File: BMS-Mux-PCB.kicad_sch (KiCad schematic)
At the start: 54 parts, among them J1 Conn_02x08_Counter_Clockwise, J2 Conn_02x08_Counter_Clockwise, J3 Conn_02x09_Counter_Clockwise, J4 Conn_01x18, J5 Conn_01x02, J6 Conn_02x10_Counter_Clockwise, Q1 BSS123, Q2 BSS123, U1 74CBTLV3257, U2 74CBTLV3257, U3 TMR_1-4812, U4 TEC2-4810WI

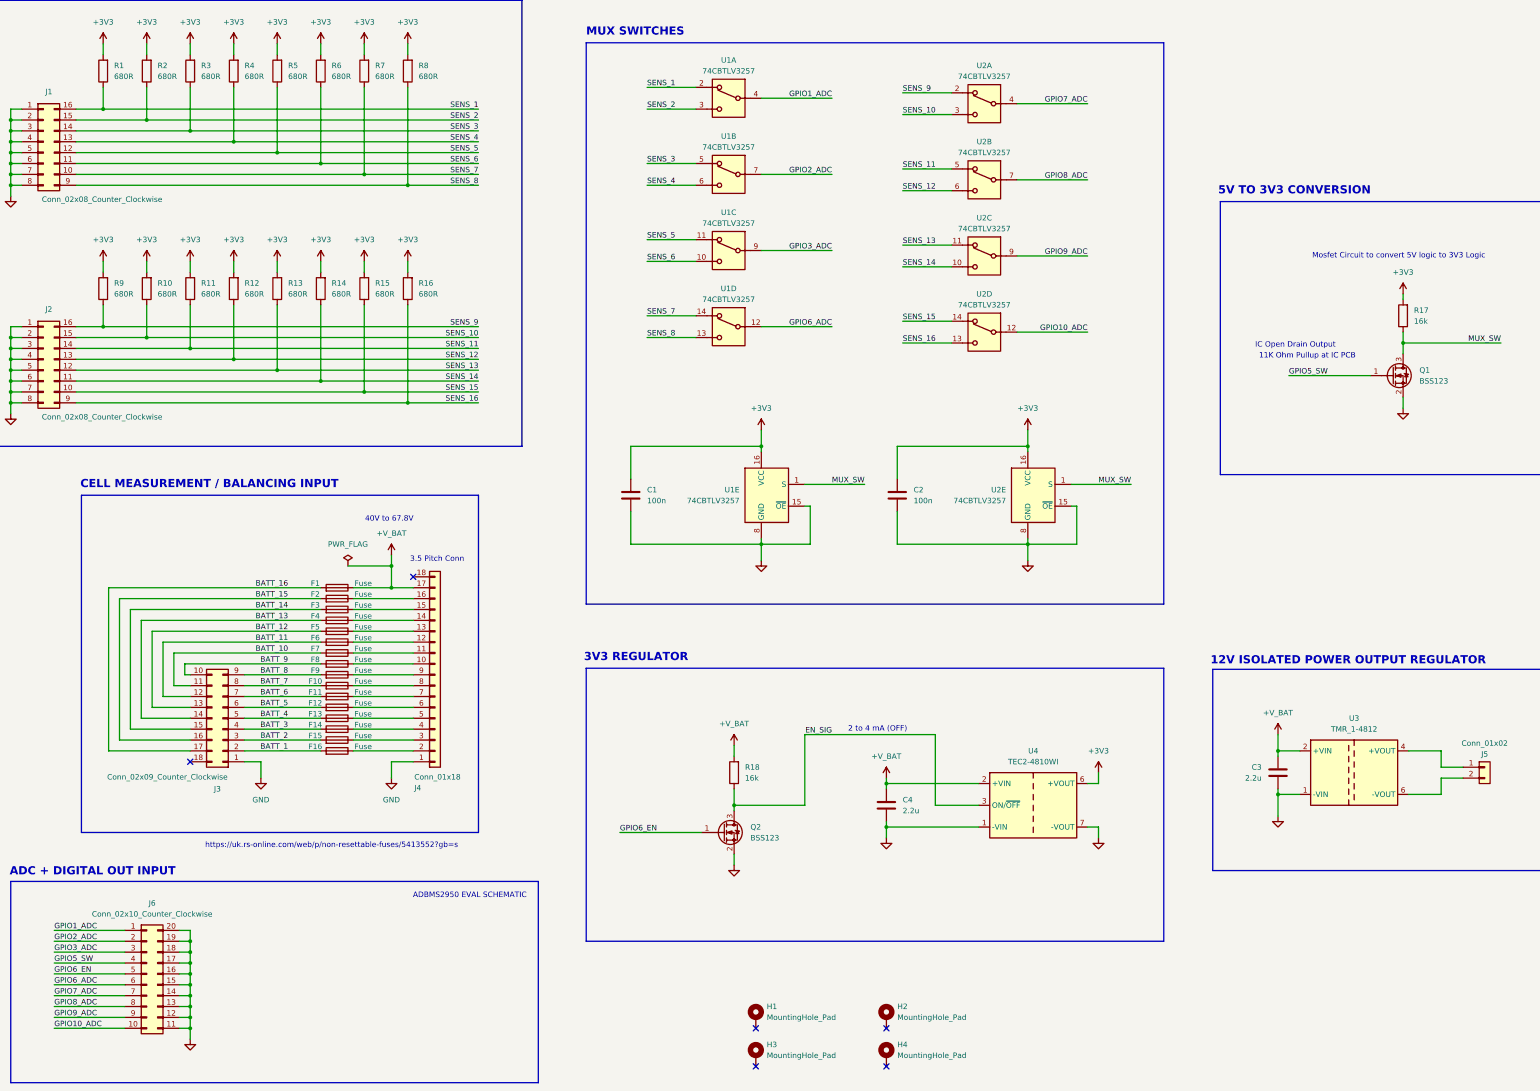
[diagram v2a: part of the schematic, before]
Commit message: updated footprints and started layout
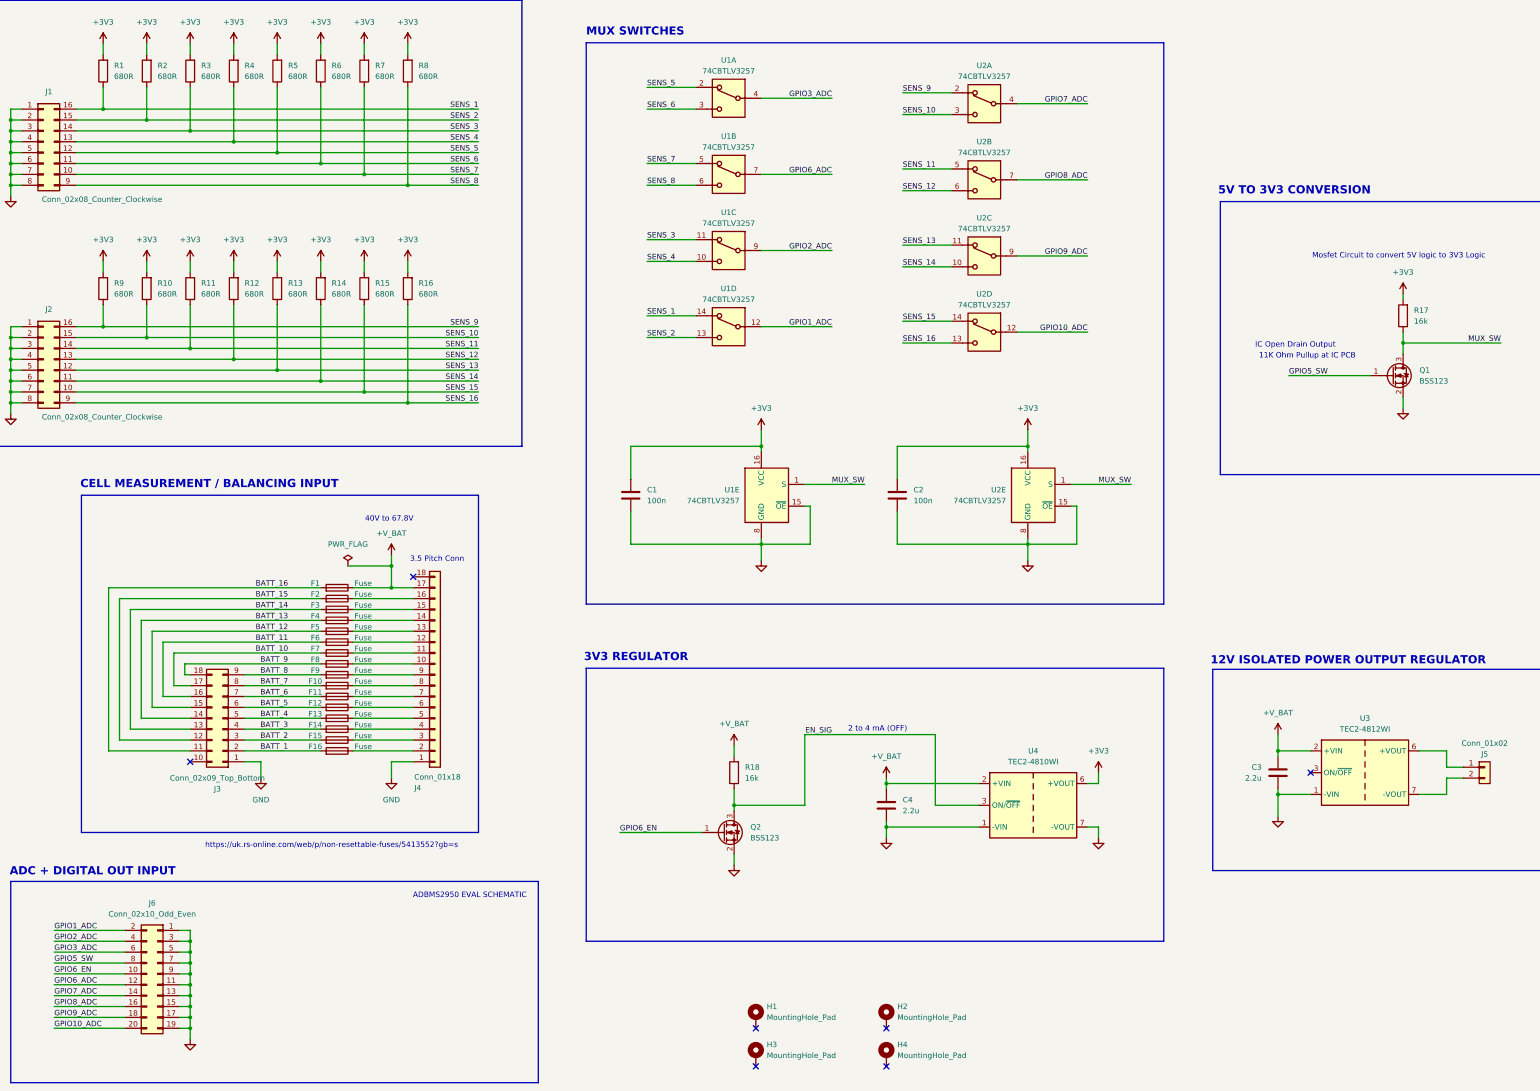
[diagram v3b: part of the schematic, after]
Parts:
- removed J3: Conn_02x09_Counter_Clockwise, Connector_Molex:Molex_Micro-Fit_3.0_43045-1800_2x09_P3.00mm_Horizontal, symbol Connector_Generic:Conn_02x09_Counter_Clockwise
- removed J6: Conn_02x10_Counter_Clockwise, Connector_PinHeader_2.54mm:PinHeader_2x10_P2.54mm_Vertical, symbol Connector_Generic:Conn_02x10_Counter_Clockwise
- removed U3: TMR_1-4812, Converter_DCDC:Converter_DCDC_TRACO_TMR-1-xxxx_Single_THT, symbol Regulator_Switching:TMR_1-4812
- added J3: Conn_02x09_Top_Bottom, BMS-Mux-footprints:Molex_Micro-Fit_3.0_43045-1800_2x09_P3.00mm_Horizontal, symbol Connector_Generic:Conn_02x09_Top_Bottom
- added J6: Conn_02x10_Odd_Even, Connector_PinHeader_2.54mm:PinHeader_2x10_P2.54mm_Vertical, symbol Connector_Generic:Conn_02x10_Odd_Even
- added U3: TEC2-4812WI, Converter_DCDC:Converter_DCDC_TRACO_TMR-xxxx_THT, symbol Converter_DCDC:TEC2-4812WI
- J1, J2: footprint Connector_Molex:Molex_Micro-Fit_3.0_43045-1600_2x08_P3.00mm_Horizontal -> BMS-Mux-footprints:Molex_Micro-Fit_3.0_43045-1600_2x08_P3.00mm_Horizontal
- J5: footprint Connector_Molex:Molex_Micro-Fit_3.0_43650-0200_1x02_P3.00mm_Horizontal -> BMS-Mux-footprints:Molex_Micro-Fit_3.0_43650-0200_1x02_P3.00mm_Horizontal
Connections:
- net +V_BAT: now also U3.2 (+VIN)
- net BATT_1: now also J3.2 (Pin_2)
- net BATT_10: now also J3.17 (Pin_17)
- net BATT_11: now also J3.16 (Pin_16)
- net BATT_12: now also J3.15 (Pin_15)
- net BATT_13: now also J3.14 (Pin_14)
- net BATT_14: now also J3.13 (Pin_13)
- net BATT_15: now also J3.12 (Pin_12)
- net BATT_16: now also J3.11 (Pin_11)
- net BATT_2: now also J3.3 (Pin_3)
- net BATT_3: now also J3.4 (Pin_4)
- net BATT_4: now also J3.5 (Pin_5)
- net BATT_5: now also J3.6 (Pin_6)
- net BATT_6: now also J3.7 (Pin_7)
- net BATT_7: now also J3.8 (Pin_8)
- net BATT_8: now also J3.9 (Pin_9)
- net BATT_9: now also J3.18 (Pin_18)
- net GND: now also J3.1 (Pin_1), J6.1 (Pin_1), J6.11 (Pin_11), J6.13 (Pin_13), J6.15 (Pin_15), J6.17 (Pin_17), J6.19 (Pin_19), J6.3 (Pin_3), J6.5 (Pin_5), J6.7 (Pin_7), J6.9 (Pin_9), U3.1 (-VIN)
- net GPIO10_ADC: now also J6.20 (Pin_20)
- net GPIO1_ADC: now also U1.12, J6.2 (Pin_2); no longer U1.4
- net GPIO2_ADC: now also U1.9, J6.4 (Pin_4); no longer U1.7
- net GPIO3_ADC: now also U1.4, J6.6 (Pin_6); no longer U1.9
- net GPIO5_SW: now also J6.8 (Pin_8)
- net GPIO6_ADC: now also U1.7, J6.12 (Pin_12); no longer U1.12
- net GPIO6_EN: now also J6.10 (Pin_10)
- net GPIO7_ADC: now also J6.14 (Pin_14)
- net GPIO8_ADC: now also J6.16 (Pin_16)
- net GPIO9_ADC: now also J6.18 (Pin_18)
- net SENS_1: now also U1.14; no longer U1.2
- net SENS_2: now also U1.13; no longer U1.3
- net SENS_3: now also U1.11; no longer U1.5
- net SENS_4: now also U1.10; no longer U1.6
- net SENS_5: now also U1.2; no longer U1.11
- net SENS_6: now also U1.3; no longer U1.10
- net SENS_7: now also U1.5; no longer U1.14
- net SENS_8: now also U1.6; no longer U1.13
- net at J5.1 (Pin_1): now also U3.6 (+VOUT)
- net at J5.2 (Pin_2): now also U3.7 (-VOUT)
- no-connect marks 6 -> 7

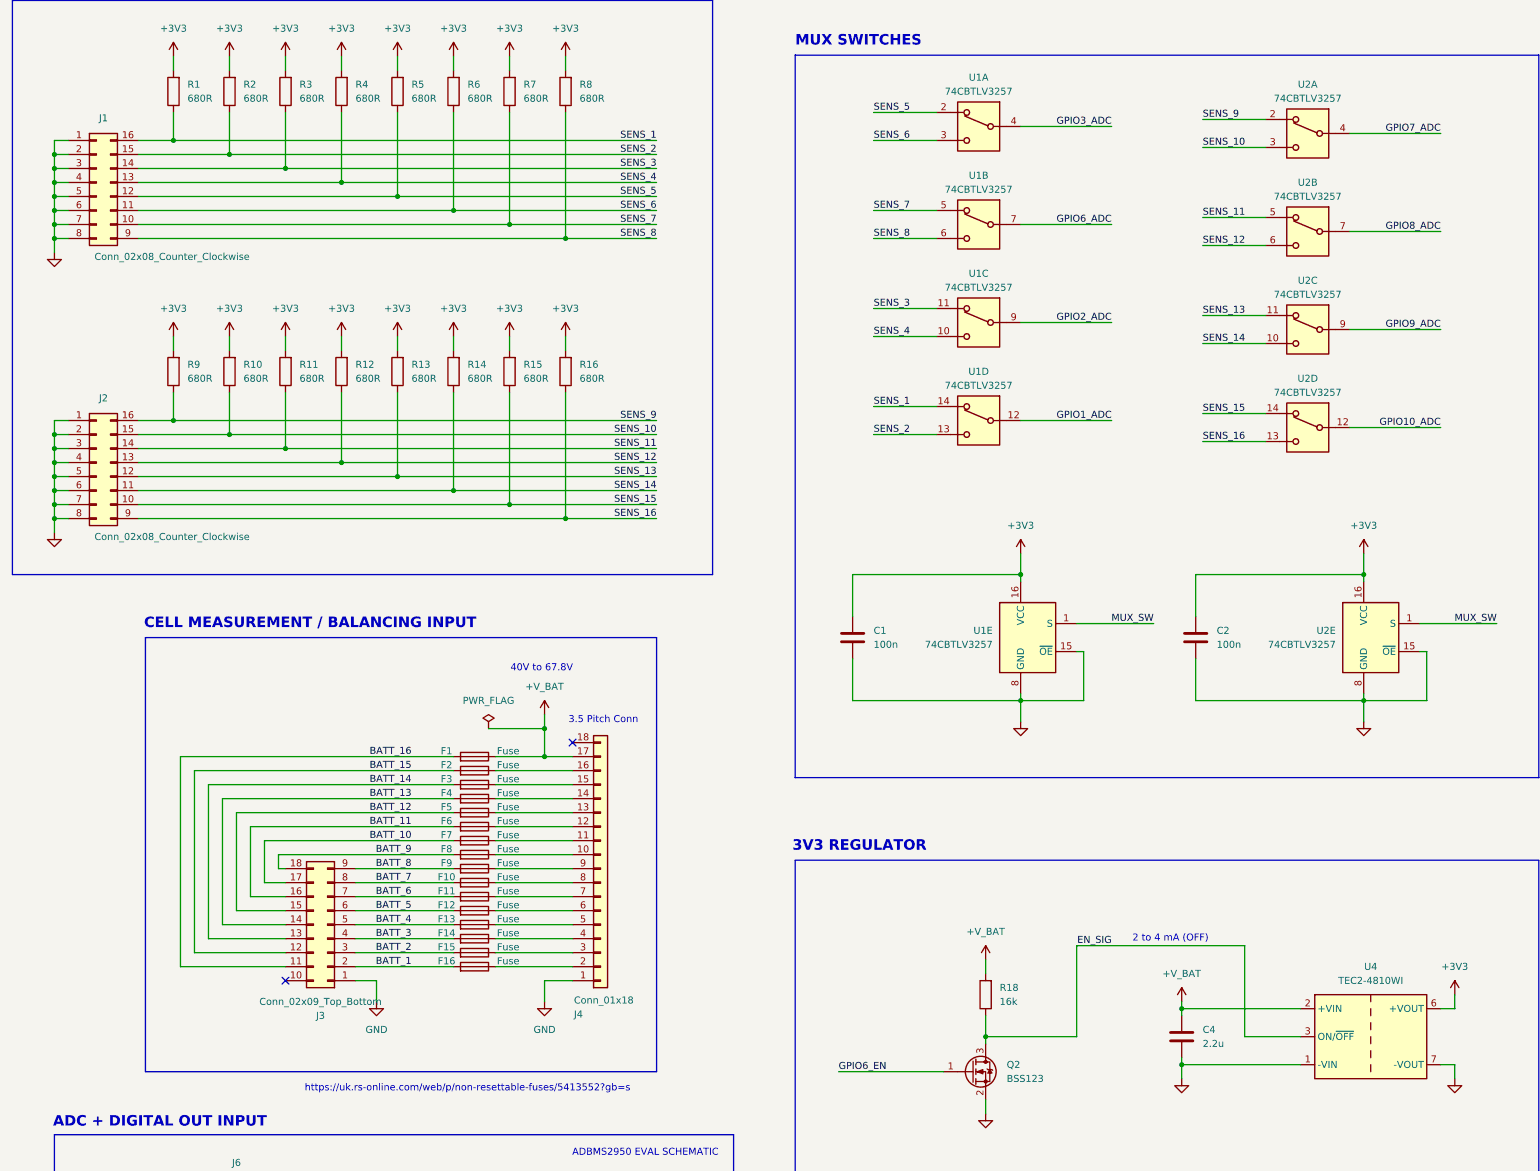
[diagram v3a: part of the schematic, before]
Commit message: changed connector orientation and halfway routed
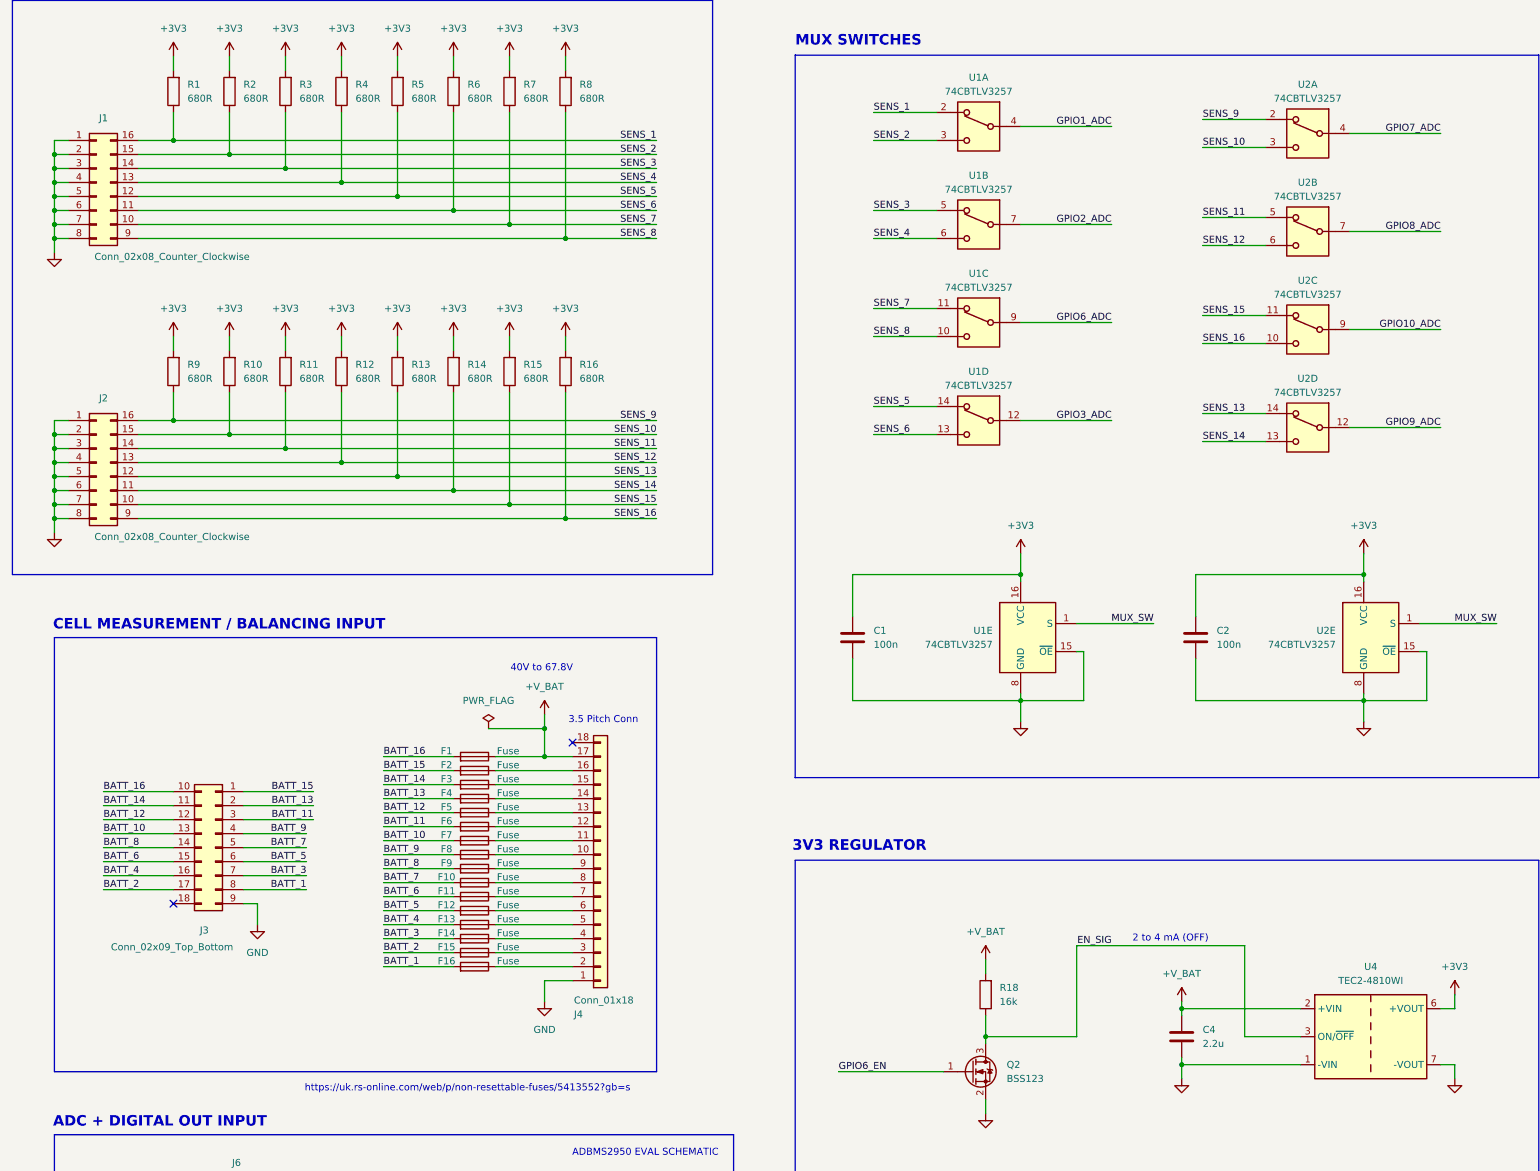
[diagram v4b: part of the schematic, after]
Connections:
- net BATT_1: now also J3.8 (Pin_8); no longer J3.2 (Pin_2)
- net BATT_10: now also J3.13 (Pin_13); no longer J3.17 (Pin_17)
- net BATT_11: now also J3.3 (Pin_3); no longer J3.16 (Pin_16)
- net BATT_12: now also J3.12 (Pin_12); no longer J3.15 (Pin_15)
- net BATT_13: now also J3.2 (Pin_2); no longer J3.14 (Pin_14)
- net BATT_14: now also J3.11 (Pin_11); no longer J3.13 (Pin_13)
- net BATT_15: now also J3.1 (Pin_1); no longer J3.12 (Pin_12)
- net BATT_16: now also J3.10 (Pin_10); no longer J3.11 (Pin_11)
- net BATT_2: now also J3.17 (Pin_17); no longer J3.3 (Pin_3)
- net BATT_3: now also J3.7 (Pin_7); no longer J3.4 (Pin_4)
- net BATT_4: now also J3.16 (Pin_16); no longer J3.5 (Pin_5)
- net BATT_6: now also J3.15 (Pin_15); no longer J3.7 (Pin_7)
- net BATT_7: now also J3.5 (Pin_5); no longer J3.8 (Pin_8)
- net BATT_8: now also J3.14 (Pin_14); no longer J3.9 (Pin_9)
- net BATT_9: now also J3.4 (Pin_4); no longer J3.18 (Pin_18)
- net GND: now also J3.9 (Pin_9); no longer J3.1 (Pin_1)
- net GPIO10_ADC: now also U2.9; no longer U2.12
- net GPIO1_ADC: now also U1.4; no longer U1.12
- net GPIO2_ADC: now also U1.7; no longer U1.9
- net GPIO3_ADC: now also U1.12; no longer U1.4
- net GPIO6_ADC: now also U1.9; no longer U1.7
- net GPIO9_ADC: now also U2.12; no longer U2.9
- net SENS_1: now also U1.2; no longer U1.14
- net SENS_13: now also U2.14; no longer U2.11
- net SENS_14: now also U2.13; no longer U2.10
- net SENS_15: now also U2.11; no longer U2.14
- net SENS_16: now also U2.10; no longer U2.13
- net SENS_2: now also U1.3; no longer U1.13
- net SENS_3: now also U1.5; no longer U1.11
- net SENS_4: now also U1.6; no longer U1.10
- net SENS_5: now also U1.14; no longer U1.2
- net SENS_6: now also U1.13; no longer U1.3
- net SENS_7: now also U1.11; no longer U1.5
- net SENS_8: now also U1.10; no longer U1.6
